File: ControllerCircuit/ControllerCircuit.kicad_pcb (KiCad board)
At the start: 2 copper layers, 122.5 x 87.5 mm, 107 parts, among them J1 ScrewTerminal, J10 Conn_01x02_Female, J12 ScrewTerminal, J14 Unused header, J15 Molex 0472192001, J2 ScrewTerminal3Pin, J3 ScrewTerminal3Pin, J4 ScrewTerminal, J5 ScrewTerminal, J7 ScrewTerminal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

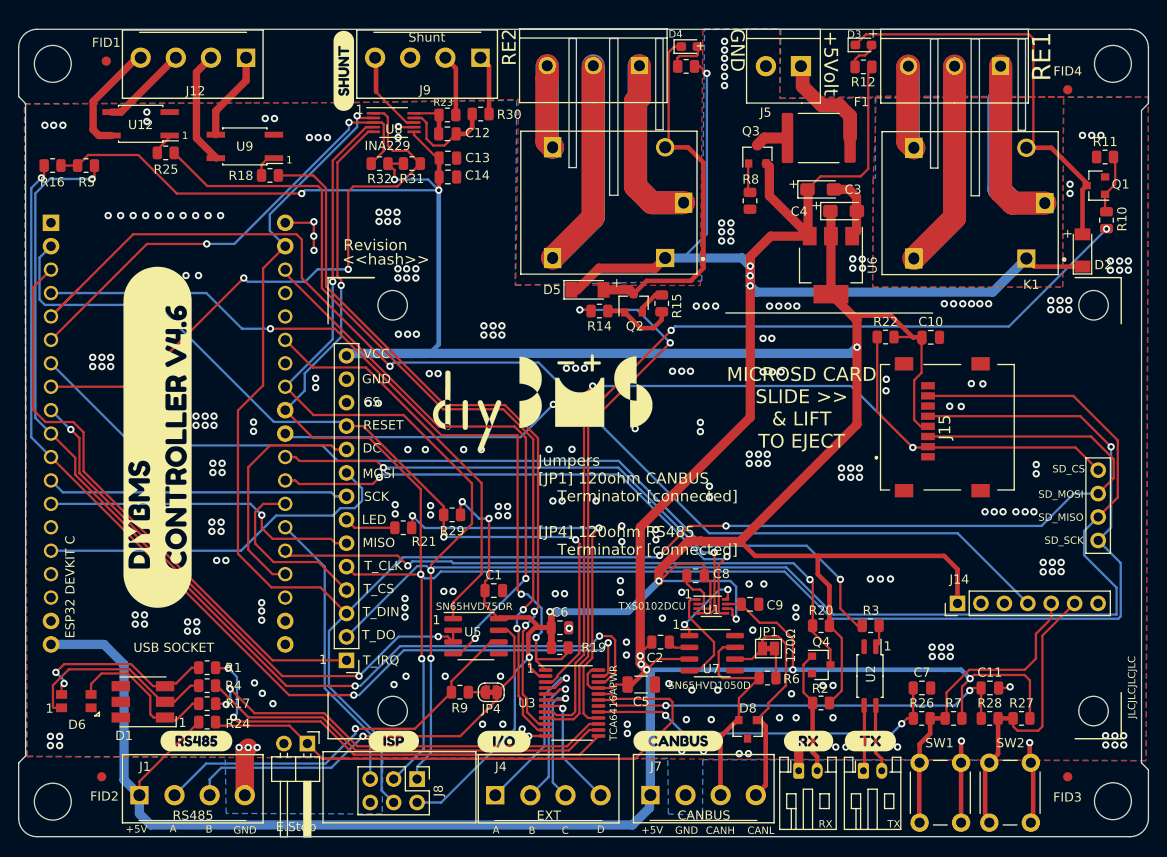
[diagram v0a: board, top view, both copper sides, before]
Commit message: prismatic diyBMS boards for LF230 / LF280 cells
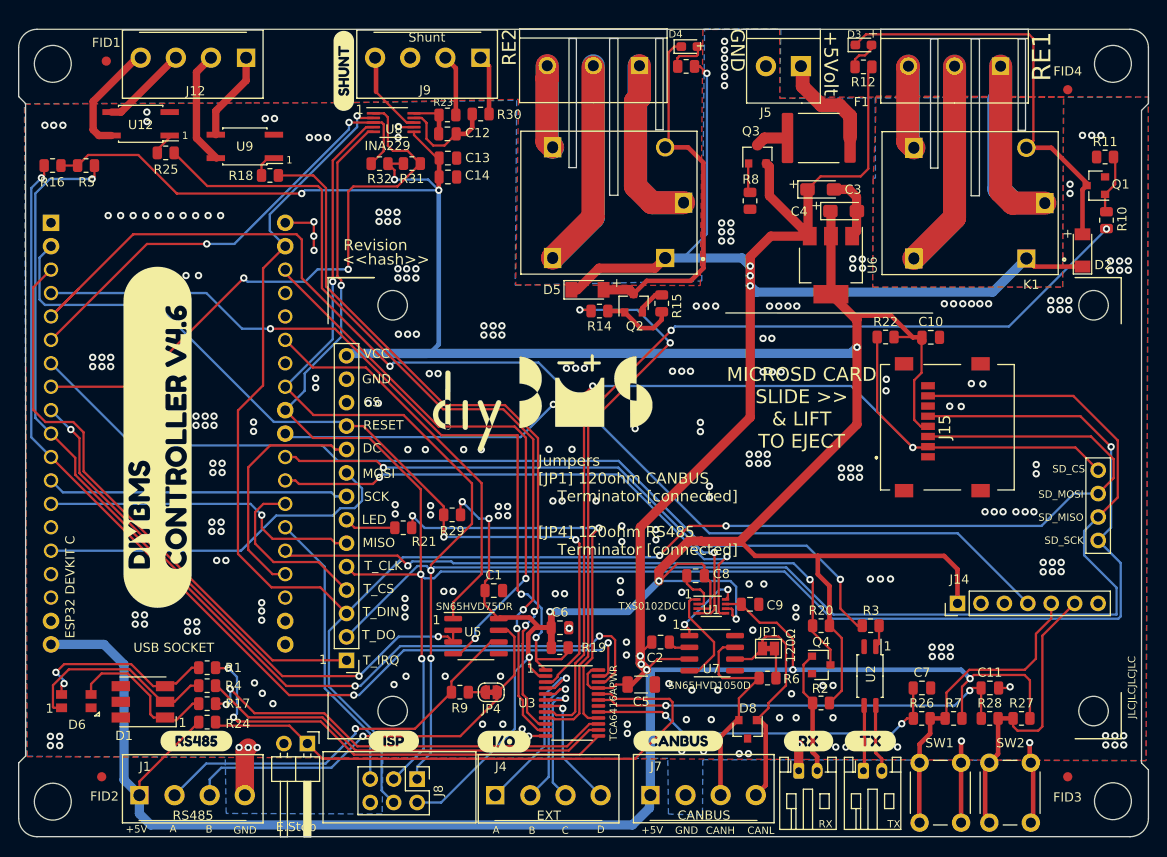
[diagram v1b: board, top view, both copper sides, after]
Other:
- net class Default removed
- net class Half mm removed
- net class High Clearance removed
- net class Relay removed
